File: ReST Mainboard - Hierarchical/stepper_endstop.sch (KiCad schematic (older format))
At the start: 34 parts, among them P10 CONN_02X04, P11 CONN_01X04, P12 CONN_01X04, P13 CONN_01X04, P14 CONN_01X04, P4 CONN_01X03, P5 CONN_01X03, P6 CONN_01X03, P7 CONN_01X03, P8 CONN_01X03, P9 CONN_01X03, U1 MCP23017, U2 POLOLU_A4988, U5 POLOLU_A4988, U6 POLOLU_A4988, U7 POLOLU_A4988, U8 POLOLU_A4988

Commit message: started routing
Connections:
- net YM1: now also U1.26 (GPA5); no longer U1.24 (GPA3)
- net YM3: now also U1.24 (GPA3); no longer U1.26 (GPA5)
- net E0_1B: now reaches P11.4 (P4), U2.3 (IB)
- net E0_1A: now reaches P11.3 (P3), U2.4 (1A)
- net E0_2A: now reaches P11.2 (P2), U2.5 (2A)
- net E0_2B: now reaches P11.1 (P1), U2.6 (2B)
- net Y_1B: now reaches P12.4 (P4), U5.3 (IB)
- net Y_1A: now reaches P12.3 (P3), U5.4 (1A)
- net Y_2A: now reaches P12.2 (P2), U5.5 (2A)
- net Y_2B: now reaches P12.1 (P1), U5.6 (2B)
- net Z_1B: now reaches P10.1 (P1), P10.2 (P2), U7.3 (IB)
- net Z_1A: now reaches P10.3 (P3), P10.4 (P4), U7.4 (1A)
- net Z_2A: now reaches P10.5 (P5), P10.6 (P6), U7.5 (2A)
- net Z_2B: now reaches P10.7 (P7), P10.8 (P8), U7.6 (2B)
- net X_1B: now reaches P13.4 (P4), U6.3 (IB)
- net X_1A: now reaches P13.3 (P3), U6.4 (1A)
- net X_2A: now reaches P13.2 (P2), U6.5 (2A)
- net X_2B: now reaches P13.1 (P1), U6.6 (2B)
- net E1_1B: now reaches P14.4 (P4), U8.3 (IB)
- net E1_1A: now reaches P14.3 (P3), U8.4 (1A)
- net E1_2A: now reaches P14.2 (P2), U8.5 (2A)
- net E1_2B: now reaches P14.1 (P1), U8.6 (2B)
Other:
- moved on the sheet: P11, P12, P13, P14
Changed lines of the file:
@@
 L CONN_01X04 P11
 U 1 1 57788622
-P 4450 950
-F 0 "P11" H 4450 1200 50  0000 C CNN
-F 1 "CONN_01X04" V 4550 950 50  0000 C CNN
-F 2 "Pin_Headers:Pin_Header_Straight_1x04" H 4450 950 50  0001 C CNN
-F 3 "" H 4450 950 50  0000 C CNN
-	1    4450 950
+P 4400 950
+F 0 "P11" H 4400 1200 50  0000 C CNN
+F 1 "CONN_01X04" V 4500 950 50  0000 C CNN
+F 2 "Pin_Headers:Pin_Header_Straight_1x04" H 4400 950 50  0001 C CNN
+F 3 "" H 4400 950 50  0000 C CNN
+	1    4400 950
 	-1   0    0    1
 $EndComp
@@
 L CONN_01X04 P12
 U 1 1 57788629
-P 4450 2600
-F 0 "P12" H 4450 2850 50  0000 C CNN
-F 1 "CONN_01X04" V 4550 2600 50  0000 C CNN
-F 2 "Pin_Headers:Pin_Header_Straight_1x04" H 4450 2600 50  0001 C CNN
-F 3 "" H 4450 2600 50  0000 C CNN
-	1    4450 2600
+P 4400 2600
+F 0 "P12" H 4400 2850 50  0000 C CNN
+F 1 "CONN_01X04" V 4500 2600 50  0000 C CNN
+F 2 "Pin_Headers:Pin_Header_Straight_1x04" H 4400 2600 50  0001 C CNN
+F 3 "" H 4400 2600 50  0000 C CNN
+	1    4400 2600
 	-1   0    0    1
 $EndComp
@@
 L CONN_01X04 P13
 U 1 1 57788630
-P 4450 4250
-F 0 "P13" H 4450 4500 50  0000 C CNN
-F 1 "CONN_01X04" V 4550 4250 50  0000 C CNN
-F 2 "Pin_Headers:Pin_Header_Straight_1x04" H 4450 4250 50  0001 C CNN
-F 3 "" H 4450 4250 50  0000 C CNN
-	1    4450 4250
+P 4400 4250
+F 0 "P13" H 4400 4500 50  0000 C CNN
+F 1 "CONN_01X04" V 4500 4250 50  0000 C CNN
+F 2 "Pin_Headers:Pin_Header_Straight_1x04" H 4400 4250 50  0001 C CNN
+F 3 "" H 4400 4250 50  0000 C CNN
+	1    4400 4250
 	-1   0    0    1
 $EndComp
@@
 Text Label 3250 4400 0    39   ~ 0
 XM1
-Text Label 3250 4500 0    39   ~ 0
+Text Label 3250 4700 0    39   ~ 0
 YM3
 Text Label 3250 4600 0    39   ~ 0
 YM2
-Text Label 3250 4700 0    39   ~ 0
+Text Label 3250 4500 0    39   ~ 0
 YM1
 Text Label 3250 4800 0    39   ~ 0
@@
 L CONN_01X04 P14
 U 1 1 5778873B
-P 4450 7550
-F 0 "P14" H 4450 7800 50  0000 C CNN
-F 1 "CONN_01X04" V 4550 7550 50  0000 C CNN
-F 2 "Pin_Headers:Pin_Header_Straight_1x04" H 4450 7550 50  0001 C CNN
-F 3 "" H 4450 7550 50  0000 C CNN
-	1    4450 7550
-	-1   0    0    1
-$EndComp
-Wire Wire Line
-	4650 7600 4850 7600
-Wire Wire Line
-	4650 7500 4850 7500
-Wire Wire Line
-	4650 7400 4850 7400
+P 4400 7550
+F 0 "P14" H 4400 7800 50  0000 C CNN
+F 1 "CONN_01X04" V 4500 7550 50  0000 C CNN
+F 2 "Pin_Headers:Pin_Header_Straight_1x04" H 4400 7550 50  0001 C CNN
+F 3 "" H 4400 7550 50  0000 C CNN
+	1    4400 7550
+	-1   0    0    1
+$EndComp
+Wire Wire Line
+	4600 7600 4850 7600
+Wire Wire Line
+	4600 7500 4850 7500
+Wire Wire Line
+	4600 7400 4850 7400
 Wire Wire Line
 	4550 7300 4850 7300
@@
 	2150 3100 2250 3100
 Wire Wire Line
-	4650 4400 4850 4400
-Wire Wire Line
-	4650 4300 4850 4300
-Wire Wire Line
-	4650 4200 4850 4200
-Wire Wire Line
-	4650 4100 4850 4100
+	4600 4400 4850 4400
+Wire Wire Line
+	4600 4300 4850 4300
+Wire Wire Line
+	4600 4200 4850 4200
+Wire Wire Line
+	4600 4100 4850 4100
 Wire Wire Line
 	4550 4000 4850 4000
@@
 	6150 6250 6050 6250
 Wire Wire Line
-	4650 2750 4850 2750
-Wire Wire Line
-	4650 2650 4850 2650
-Wire Wire Line
-	4650 2550 4850 2550
-Wire Wire Line
-	4650 2450 4850 2450
+	4600 2750 4850 2750
+Wire Wire Line
+	4600 2650 4850 2650
+Wire Wire Line
+	4600 2550 4850 2550
+Wire Wire Line
+	4600 2450 4850 2450
 Wire Wire Line
 	4550 2350 4850 2350
@@
 	1900 5100 1900 5050
 Wire Wire Line
-	4650 800  4850 800
-Wire Wire Line
-	4850 900  4650 900
-Wire Wire Line
-	4650 1000 4850 1000
-Wire Wire Line
-	4850 1100 4650 1100
-Wire Wire Line
-	4650 7700 4850 7700
+	4600 800  4850 800
+Wire Wire Line
+	4850 900  4600 900
+Wire Wire Line
+	4600 1000 4850 1000
+Wire Wire Line
+	4850 1100 4600 1100
+Wire Wire Line
+	4600 7700 4850 7700
 Wire Notes Line
 	7100 8500 7100 250
@@
 Text GLabel 2100 900  3    39   Input ~ 0
 ENDSTOP_X_MIN
+Text Label 4650 4100 0    39   ~ 0
+X_1B
+Text Label 4650 4200 0    39   ~ 0
+X_1A
+Text Label 4650 4300 0    39   ~ 0
+X_2A
+Text Label 4650 4400 0    39   ~ 0
+X_2B
+Text Label 4650 2450 0    39   ~ 0
+Y_1B
+Text Label 4650 2550 0    39   ~ 0
+Y_1A
+Text Label 4650 2650 0    39   ~ 0
+Y_2A
+Text Label 4650 2750 0    39   ~ 0
+Y_2B
+Text Label 4650 800  0    39   ~ 0
+E0_1B
+Text Label 4650 900  0    39   ~ 0
+E0_1A
+Text Label 4650 1000 0    39   ~ 0
+E0_2A
+Text Label 4650 1100 0    39   ~ 0
+E0_2B
+Text Label 4650 7400 0    39   ~ 0
+E1_1B
+Text Label 4650 7500 0    39   ~ 0
+E1_1A
+Text Label 4650 7600 0    39   ~ 0
+E1_2A
+Text Label 4650 7700 0    39   ~ 0
+E1_2B
+Text Label 4650 5750 0    39   ~ 0
+Z_1B
+Text Label 4650 5850 0    39   ~ 0
+Z_1A
+Text Label 4650 5950 0    39   ~ 0
+Z_2A
+Text Label 4650 6050 0    39   ~ 0
+Z_2B
 $EndSCHEMATC

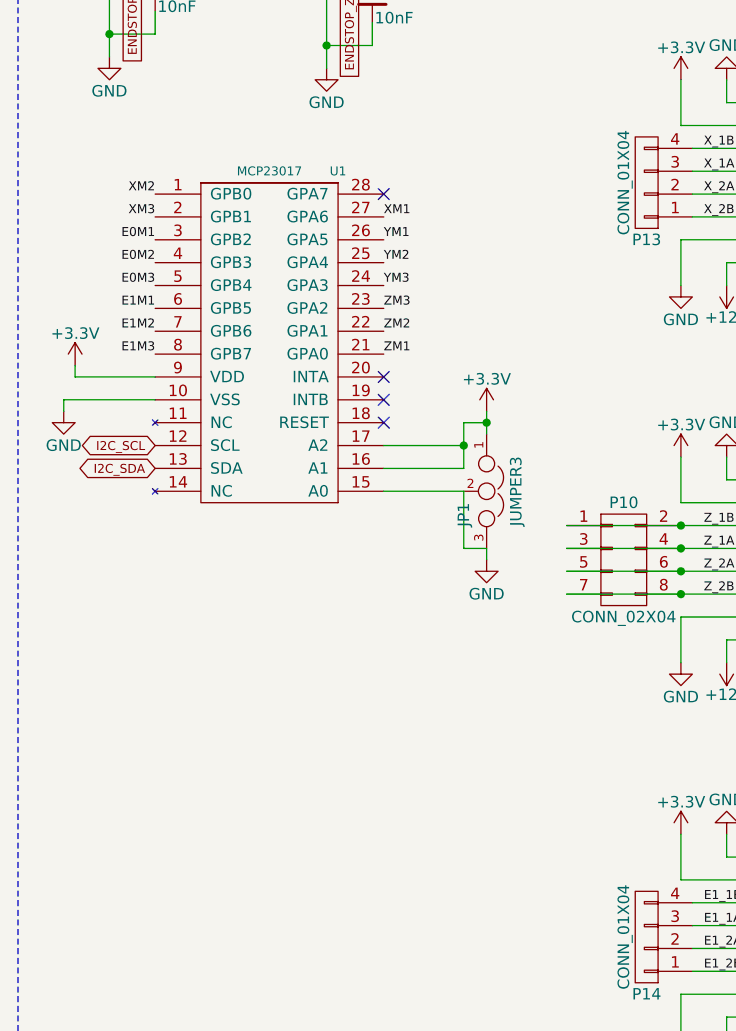
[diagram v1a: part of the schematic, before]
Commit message: Mostly finished with main PCB. Only need to work the High Current Stuff out. On Vacation for now
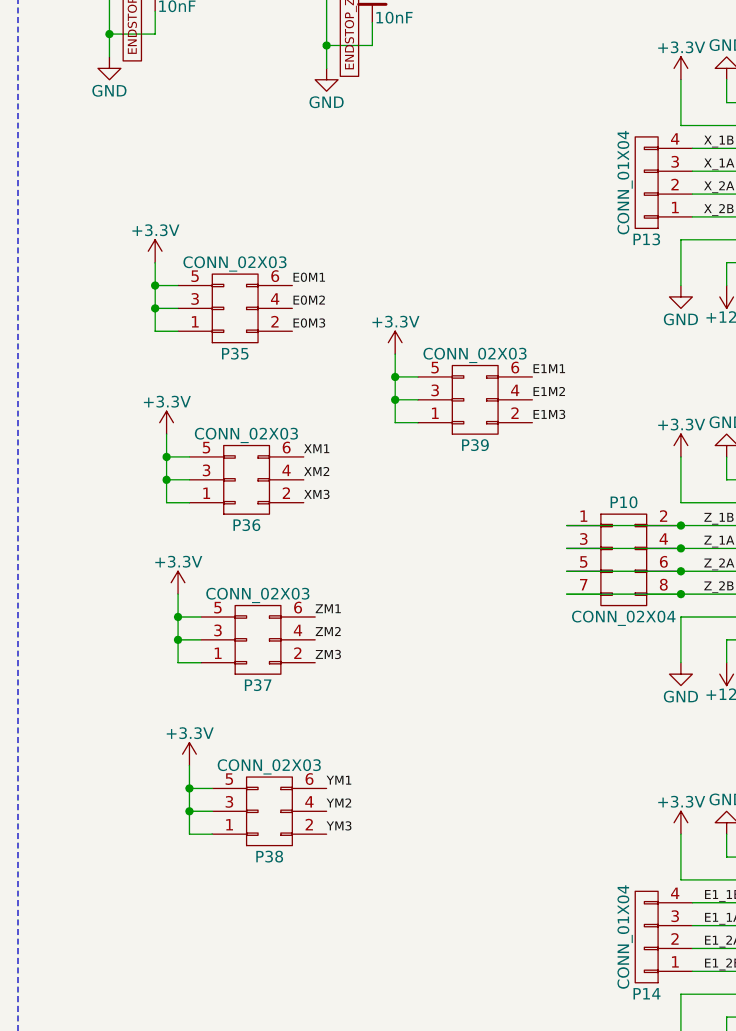
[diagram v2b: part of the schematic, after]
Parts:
- removed JP1: JUMPER3, ReST-Library:S_JUMPER_3, symbol JUMPER3
- removed U1: MCP23017, Housings_SSOP:SSOP-28_5.3x10.2mm_Pitch0.65mm, symbol MCP23017
- added P35, P36, P37, P38, P39: CONN_02X03, ReST-Library:bb02-hp06, symbol CONN_02X03
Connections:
- net +3V3: now also P35.1 (P1), P35.3 (P3), P35.5 (P5), P36.1 (P1), P36.3 (P3), P36.5 (P5), P37.1 (P1), P37.3 (P3), P37.5 (P5), P38.1 (P1), P38.3 (P3), P38.5 (P5), P39.1 (P1), P39.3 (P3), P39.5 (P5)
- net E0M1: now also P35.6 (P6)
- net E0M2: now also P35.4 (P4)
- net E0M3: now also P35.2 (P2)
- net E1M1: now also P39.6 (P6)
- net E1M2: now also P39.4 (P4)
- net E1M3: now also P39.2 (P2)
- net XM1: now also P36.6 (P6)
- net XM2: now also P36.4 (P4)
- net XM3: now also P36.2 (P2)
- net YM1: now also P38.6 (P6)
- net YM2: now also P38.4 (P4)
- net YM3: now also P38.2 (P2)
- net ZM1: now also P37.6 (P6)
- net ZM2: now also P37.4 (P4)
- net ZM3: now also P37.2 (P2)
- no-connect marks 4 -> 0
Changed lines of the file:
@@
 	-1   0    0    1
-$EndComp
-$Comp
-L MCP23017 U1
-U 1 1 577886F1
-P 2750 4800
-F 0 "U1" H 3050 5400 39  0000 C CNN
-F 1 "MCP23017" H 2750 5400 39  0000 C CNN
-F 2 "Housings_SSOP:SSOP-28_5.3x10.2mm_Pitch0.65mm" H 2450 5400 39  0001 C CNN
-F 3 "" H 2450 5400 39  0000 C CNN
-	1    2750 4800
-	1    0    0    -1
 $EndComp
 Text Label 6050 5950 0    39   ~ 0
@@
 Text Label 6050 7800 0    39   ~ 0
 E1M1
-$Comp
-L +3.3V #PWR0109
-U 1 1 57788709
-P 3700 5250
-F 0 "#PWR0109" H 3700 5100 50  0001 C CNN
-F 1 "+3.3V" H 3700 5390 50  0000 C CNN
-F 2 "" H 3700 5250 50  0000 C CNN
-F 3 "" H 3700 5250 50  0000 C CNN
-	1    3700 5250
-	1    0    0    -1
-$EndComp
-$Comp
-L GND #PWR0110
-U 1 1 5778870F
-P 3700 5900
-F 0 "#PWR0110" H 3700 5650 50  0001 C CNN
-F 1 "GND" H 3700 5750 50  0000 C CNN
-F 2 "" H 3700 5900 50  0000 C CNN
-F 3 "" H 3700 5900 50  0000 C CNN
-	1    3700 5900
-	1    0    0    -1
-$EndComp
-$Comp
-L JUMPER3 JP1
-U 1 1 57788715
-P 3700 5600
-F 0 "JP1" H 3750 5500 50  0000 L CNN
-F 1 "JUMPER3" H 3700 5700 50  0000 C BNN
-F 2 "ReST-Library:S_JUMPER_3" H 3700 5600 50  0001 C CNN
-F 3 "" H 3700 5600 50  0000 C CNN
-	1    3700 5600
-	0    1    1    0
-$EndComp
-$Comp
-L +3.3V #PWR0111
-U 1 1 5778871C
-P 1900 5050
-F 0 "#PWR0111" H 1900 4900 50  0001 C CNN
-F 1 "+3.3V" H 1900 5190 50  0000 C CNN
-F 2 "" H 1900 5050 50  0000 C CNN
-F 3 "" H 1900 5050 50  0000 C CNN
-	1    1900 5050
-	1    0    0    -1
-$EndComp
-$Comp
-L GND #PWR0112
-U 1 1 57788722
-P 1850 5250
-F 0 "#PWR0112" H 1850 5000 50  0001 C CNN
-F 1 "GND" H 1850 5100 50  0000 C CNN
-F 2 "" H 1850 5250 50  0000 C CNN
-F 3 "" H 1850 5250 50  0000 C CNN
-	1    1850 5250
-	1    0    0    -1
-$EndComp
-Text Label 2250 4400 2    39   ~ 0
+Text Label 2900 5650 0    39   ~ 0
 XM3
-Text Label 2250 4300 2    39   ~ 0
+Text Label 2900 5550 0    39   ~ 0
 XM2
-Text Label 3250 4400 0    39   ~ 0
+Text Label 2900 5450 0    39   ~ 0
 XM1
-Text Label 3250 4700 0    39   ~ 0
+Text Label 3000 7100 0    39   ~ 0
 YM3
-Text Label 3250 4600 0    39   ~ 0
+Text Label 3000 7000 0    39   ~ 0
 YM2
-Text Label 3250 4500 0    39   ~ 0
+Text Label 3000 6900 0    39   ~ 0
 YM1
-Text Label 3250 4800 0    39   ~ 0
+Text Label 2950 6350 0    39   ~ 0
 ZM3
-Text Label 3250 4900 0    39   ~ 0
+Text Label 2950 6250 0    39   ~ 0
 ZM2
-Text Label 3250 5000 0    39   ~ 0
+Text Label 2950 6150 0    39   ~ 0
 ZM1
-Text Label 2250 5000 2    39   ~ 0
+Text Label 3900 5300 0    39   ~ 0
 E1M3
-Text Label 2250 4900 2    39   ~ 0
+Text Label 3900 5200 0    39   ~ 0
 E1M2
-Text Label 2250 4800 2    39   ~ 0
+Text Label 3900 5100 0    39   ~ 0
 E1M1
-NoConn ~ 3250 5100
-NoConn ~ 3250 5200
-NoConn ~ 3250 5300
-NoConn ~ 3250 4300
-Text Label 2250 4500 2    39   ~ 0
+Text Label 2850 4700 0    39   ~ 0
 E0M1
-Text Label 2250 4600 2    39   ~ 0
+Text Label 2850 4800 0    39   ~ 0
 E0M2
-Text Label 2250 4700 2    39   ~ 0
+Text Label 2850 4900 0    39   ~ 0
 E0M3
 $Comp
@@
 	6350 7800 6050 7800
 Wire Wire Line
-	3700 5900 3700 5850
-Wire Wire Line
-	3250 5600 3600 5600
-Wire Wire Line
-	3700 5250 3700 5350
-Wire Wire Line
-	3600 5500 3250 5500
-Wire Wire Line
-	3600 5300 3600 5500
-Wire Wire Line
-	3600 5300 3700 5300
-Connection ~ 3700 5300
-Wire Wire Line
-	3250 5400 3600 5400
-Connection ~ 3600 5400
-Wire Wire Line
-	2250 5200 1850 5200
-Wire Wire Line
-	1850 5200 1850 5250
-Wire Wire Line
-	2250 5100 1900 5100
-Wire Wire Line
-	1900 5100 1900 5050
-Wire Wire Line
 	4600 800  4850 800
 Wire Wire Line
@@
 Wire Notes Line
 	7100 250  1650 250
-Wire Wire Line
-	3700 5850 3600 5850
-Wire Wire Line
-	3600 5850 3600 5600
 Text GLabel 6150 3900 2    39   Input ~ 0
 STEPPER_X_DIR
@@
 Text GLabel 6150 7900 2    39   Input ~ 0
 STEPPER_E_1_EN
-Text GLabel 2250 5400 0    39   BiDi ~ 0
-I2C_SCL
-Text GLabel 2250 5500 0    39   BiDi ~ 0
-I2C_SDA
 Text GLabel 3100 3250 3    39   Input ~ 0
 ENDSTOP_Z_MAX
@@
 Text Label 4650 6050 0    39   ~ 0
 Z_2B
+$Comp
+L CONN_02X03 P37
+U 1 1 57767E08
+P 2700 6250
+F 0 "P37" H 2700 6450 50  0000 C CNN
+F 1 "CONN_02X03" H 2700 6050 50  0000 C CNN
+F 2 "ReST-Library:bb02-hp06" H 2700 5050 50  0001 C CNN
+F 3 "" H 2700 5050 50  0000 C CNN
+	1    2700 6250
+	1    0    0    1
+$EndComp
+Wire Wire Line
+	2350 6050 2350 6350
+Wire Wire Line
+	2350 6150 2450 6150
+Wire Wire Line
+	2350 6250 2450 6250
+Connection ~ 2350 6150
+Wire Wire Line
+	2350 6350 2450 6350
+Connection ~ 2350 6250
+$Comp
+L CONN_02X03 P38
+U 1 1 5776A0FD
+P 2750 7000
+F 0 "P38" H 2750 7200 50  0000 C CNN
+F 1 "CONN_02X03" H 2750 6800 50  0000 C CNN
+F 2 "ReST-Library:bb02-hp06" H 2750 5800 50  0001 C CNN
+F 3 "" H 2750 5800 50  0000 C CNN
+	1    2750 7000
+	1    0    0    1
+$EndComp
+$Comp
+L +3.3V #PWR0109
+U 1 1 5776A103
+P 2400 6800
+F 0 "#PWR0109" H 2400 6650 50  0001 C CNN
+F 1 "+3.3V" H 2400 6940 50  0000 C CNN
+F 2 "" H 2400 6800 50  0000 C CNN
+F 3 "" H 2400 6800 50  0000 C CNN
+	1    2400 6800
+	1    0    0    -1
+$EndComp
+Wire Wire Line
+	2400 6800 2400 7100
+Wire Wire Line
+	2400 6900 2500 6900
+Wire Wire Line
+	2400 7000 2500 7000
+Connection ~ 2400 6900
+Wire Wire Line
+	2400 7100 2500 7100
+Connection ~ 2400 7000
+$Comp
+L +3.3V #PWR0110
+U 1 1 5776A2C6
+P 2350 6050
+F 0 "#PWR0110" H 2350 5900 50  0001 C CNN
+F 1 "+3.3V" H 2350 6190 50  0000 C CNN
+F 2 "" H 2350 6050 50  0000 C CNN
+F 3 "" H 2350 6050 50  0000 C CNN
+	1    2350 6050
+	1    0    0    -1
+$EndComp
+$Comp
+L CONN_02X03 P36
+U 1 1 5776A787
+P 2650 5550
+F 0 "P36" H 2650 5750 50  0000 C CNN
+F 1 "CONN_02X03" H 2650 5350 50  0000 C CNN
+F 2 "ReST-Library:bb02-hp06" H 2650 4350 50  0001 C CNN
+F 3 "" H 2650 4350 50  0000 C CNN
+	1    2650 5550
+	1    0    0    1
+$EndComp
+$Comp
+L +3.3V #PWR0111
+U 1 1 5776A78D
+P 2300 5350
+F 0 "#PWR0111" H 2300 5200 50  0001 C CNN
+F 1 "+3.3V" H 2300 5490 50  0000 C CNN
+F 2 "" H 2300 5350 50  0000 C CNN
+F 3 "" H 2300 5350 50  0000 C CNN
+	1    2300 5350
+	1    0    0    -1
+$EndComp
+Wire Wire Line
+	2300 5350 2300 5650
+Wire Wire Line
+	2300 5450 2400 5450
+Wire Wire Line
+	2300 5550 2400 5550
+Connection ~ 2300 5450
+Wire Wire Line
+	2300 5650 2400 5650
+Connection ~ 2300 5550
+$Comp
+L CONN_02X03 P35
+U 1 1 5776A7F6
+P 2600 4800
+F 0 "P35" H 2600 5000 50  0000 C CNN
+F 1 "CONN_02X03" H 2600 4600 50  0000 C CNN
+F 2 "ReST-Library:bb02-hp06" H 2600 3600 50  0001 C CNN
+F 3 "" H 2600 3600 50  0000 C CNN
+	1    2600 4800
+	1    0    0    1
+$EndComp
+$Comp
+L +3.3V #PWR0112
+U 1 1 5776A7FC
+P 2250 4600
+F 0 "#PWR0112" H 2250 4450 50  0001 C CNN
+F 1 "+3.3V" H 2250 4740 50  0000 C CNN
+F 2 "" H 2250 4600 50  0000 C CNN
+F 3 "" H 2250 4600 50  0000 C CNN
+	1    2250 4600
+	1    0    0    -1
+$EndComp
+Wire Wire Line
+	2250 4600 2250 4900
+Wire Wire Line
+	2250 4700 2350 4700
+Wire Wire Line
+	2250 4800 2350 4800
+Connection ~ 2250 4700
+Wire Wire Line
+	2250 4900 2350 4900
+Connection ~ 2250 4800
+$Comp
+L CONN_02X03 P39
+U 1 1 5776AA3D
+P 3650 5200
+F 0 "P39" H 3650 5400 50  0000 C CNN
+F 1 "CONN_02X03" H 3650 5000 50  0000 C CNN
+F 2 "ReST-Library:bb02-hp06" H 3650 4000 50  0001 C CNN
+F 3 "" H 3650 4000 50  0000 C CNN
+	1    3650 5200
+	1    0    0    1
+$EndComp
+$Comp
+L +3.3V #PWR0113
+U 1 1 5776AA43
+P 3300 5000
+F 0 "#PWR0113" H 3300 4850 50  0001 C CNN
+F 1 "+3.3V" H 3300 5140 50  0000 C CNN
+F 2 "" H 3300 5000 50  0000 C CNN
+F 3 "" H 3300 5000 50  0000 C CNN
+	1    3300 5000
+	1    0    0    -1
+$EndComp
+Wire Wire Line
+	3300 5000 3300 5300
+Wire Wire Line
+	3300 5100 3400 5100
+Wire Wire Line
+	3300 5200 3400 5200
+Connection ~ 3300 5100
+Wire Wire Line
+	3300 5300 3400 5300
+Connection ~ 3300 5200
 $EndSCHEMATC
